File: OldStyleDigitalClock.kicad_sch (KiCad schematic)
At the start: 81 parts, among them SW1 Set minutes, SW2 Set hours, U1 D168K, U10 D168K, U11 CD4026BE, U12 D168K, U13 CD4026BE, U2 CD4026BE, U3 CD4060BE, U4 D168K, U5 CD4026BE, U6 CD4017BE, U7 CD4017BE, U8 CD4017BE, U9 4073, Y1 HC49 XTAL (32768 Hz)

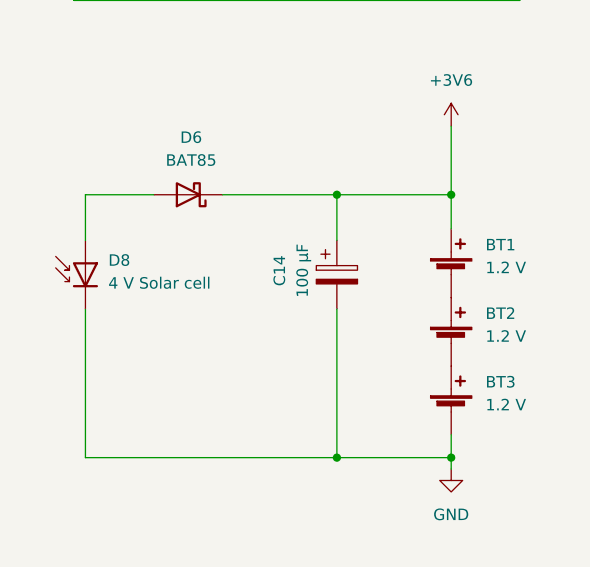
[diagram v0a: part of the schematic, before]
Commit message: Using 5 V solar cell instead of 4 V, as more appropriate for indoor situations
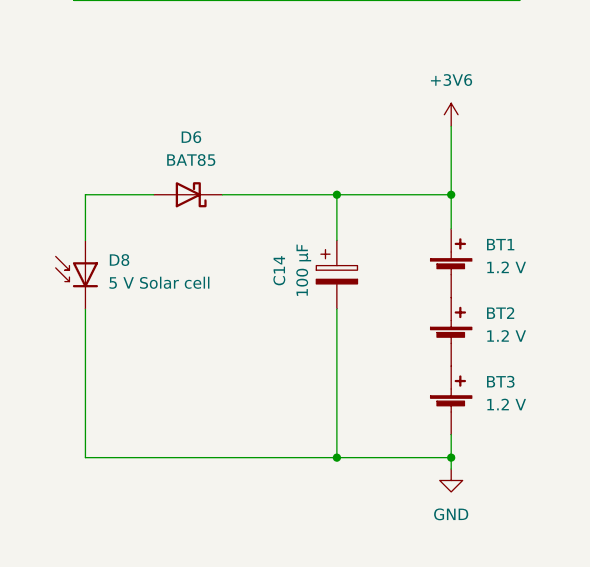
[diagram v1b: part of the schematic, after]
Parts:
- D8: value 4 V Solar cell -> 5 V Solar cell
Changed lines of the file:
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@@
       (effects (font (size 1.27 1.27)) (justify right))
     )
-    (property "Value" "4 V Solar cell" (id 1) (at 24.13 180.0224 90)
+    (property "Value" "5 V Solar cell" (id 1) (at 24.13 180.0224 90)
       (effects (font (size 1.27 1.27)) (justify right))
     )
@@
     )
     (path "/9a8343d9-4301-4fa0-a6a0-ed6d3137e10a"
-      (reference "D8") (unit 1) (value "4 V Solar cell") (footprint "TerminalBlock:TerminalBlock_bornier-2_P5.08mm")
+      (reference "D8") (unit 1) (value "5 V Solar cell") (footprint "TerminalBlock:TerminalBlock_bornier-2_P5.08mm")
     )
     (path "/0ff46600-2d15-4423-b669-8d7963d756aa"

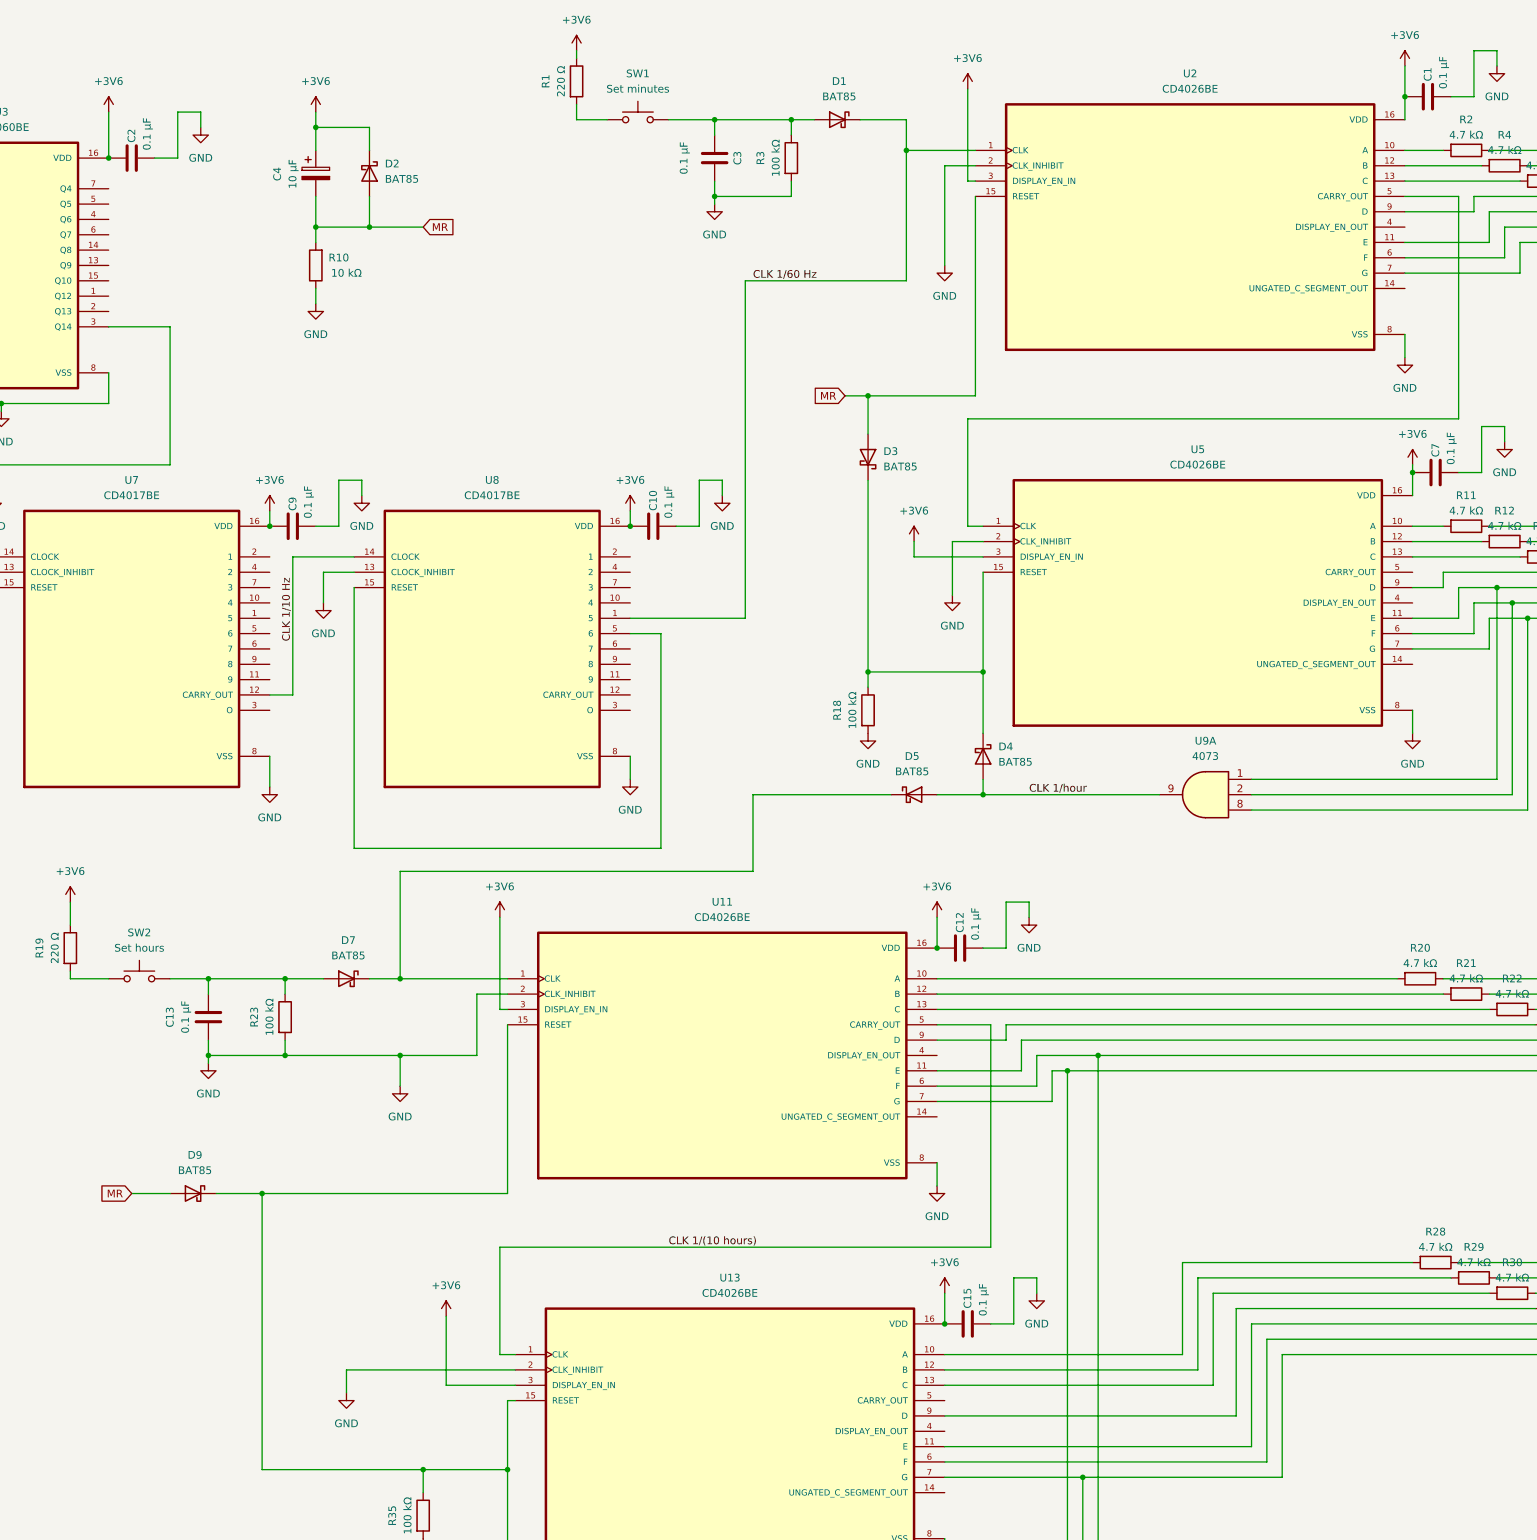
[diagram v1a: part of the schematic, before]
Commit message: Using 512 Hz clock signal to rapidly turn on and off the LEDs via the CD4026 display enable pin, both saving 50% power and hopefully improving the battery charging. The LED attenuation is negligible. This means than during the low state of the cycle, all the current from solar panels flows into the batteries, achieving a sort of trickle charging.
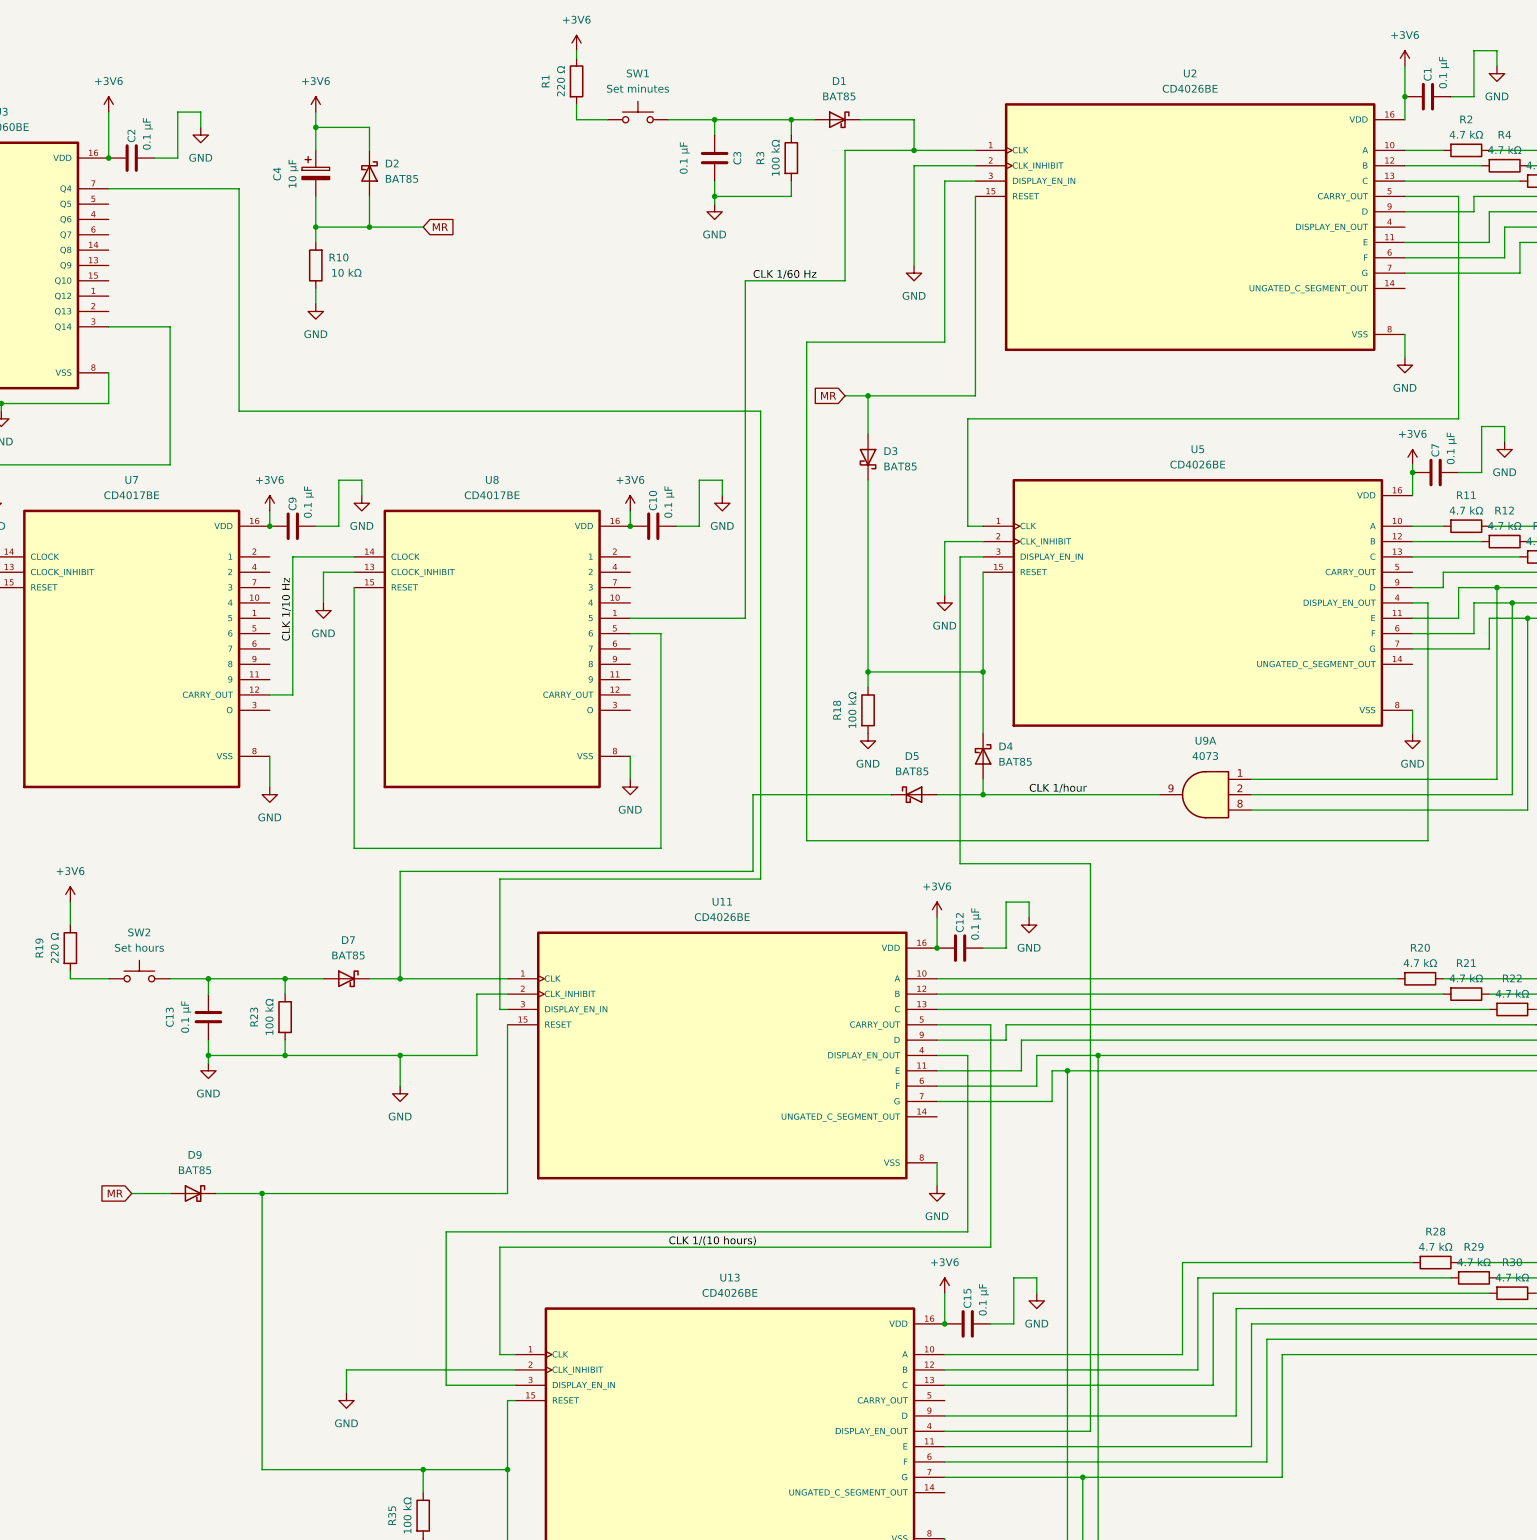
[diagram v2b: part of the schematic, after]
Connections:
- net VDD: no longer U11.3 (DISPLAY_EN_IN), U13.3 (DISPLAY_EN_IN), U2.3 (DISPLAY_EN_IN), U5.3 (DISPLAY_EN_IN)
- net at U11.4 (DISPLAY_EN_OUT): now also U13.3 (DISPLAY_EN_IN)
- net at U5.4 (DISPLAY_EN_OUT): now also U2.3 (DISPLAY_EN_IN)
- net at U13.4 (DISPLAY_EN_OUT): now also U5.3 (DISPLAY_EN_IN)
- net at U3.7 (Q4): now also U11.3 (DISPLAY_EN_IN)

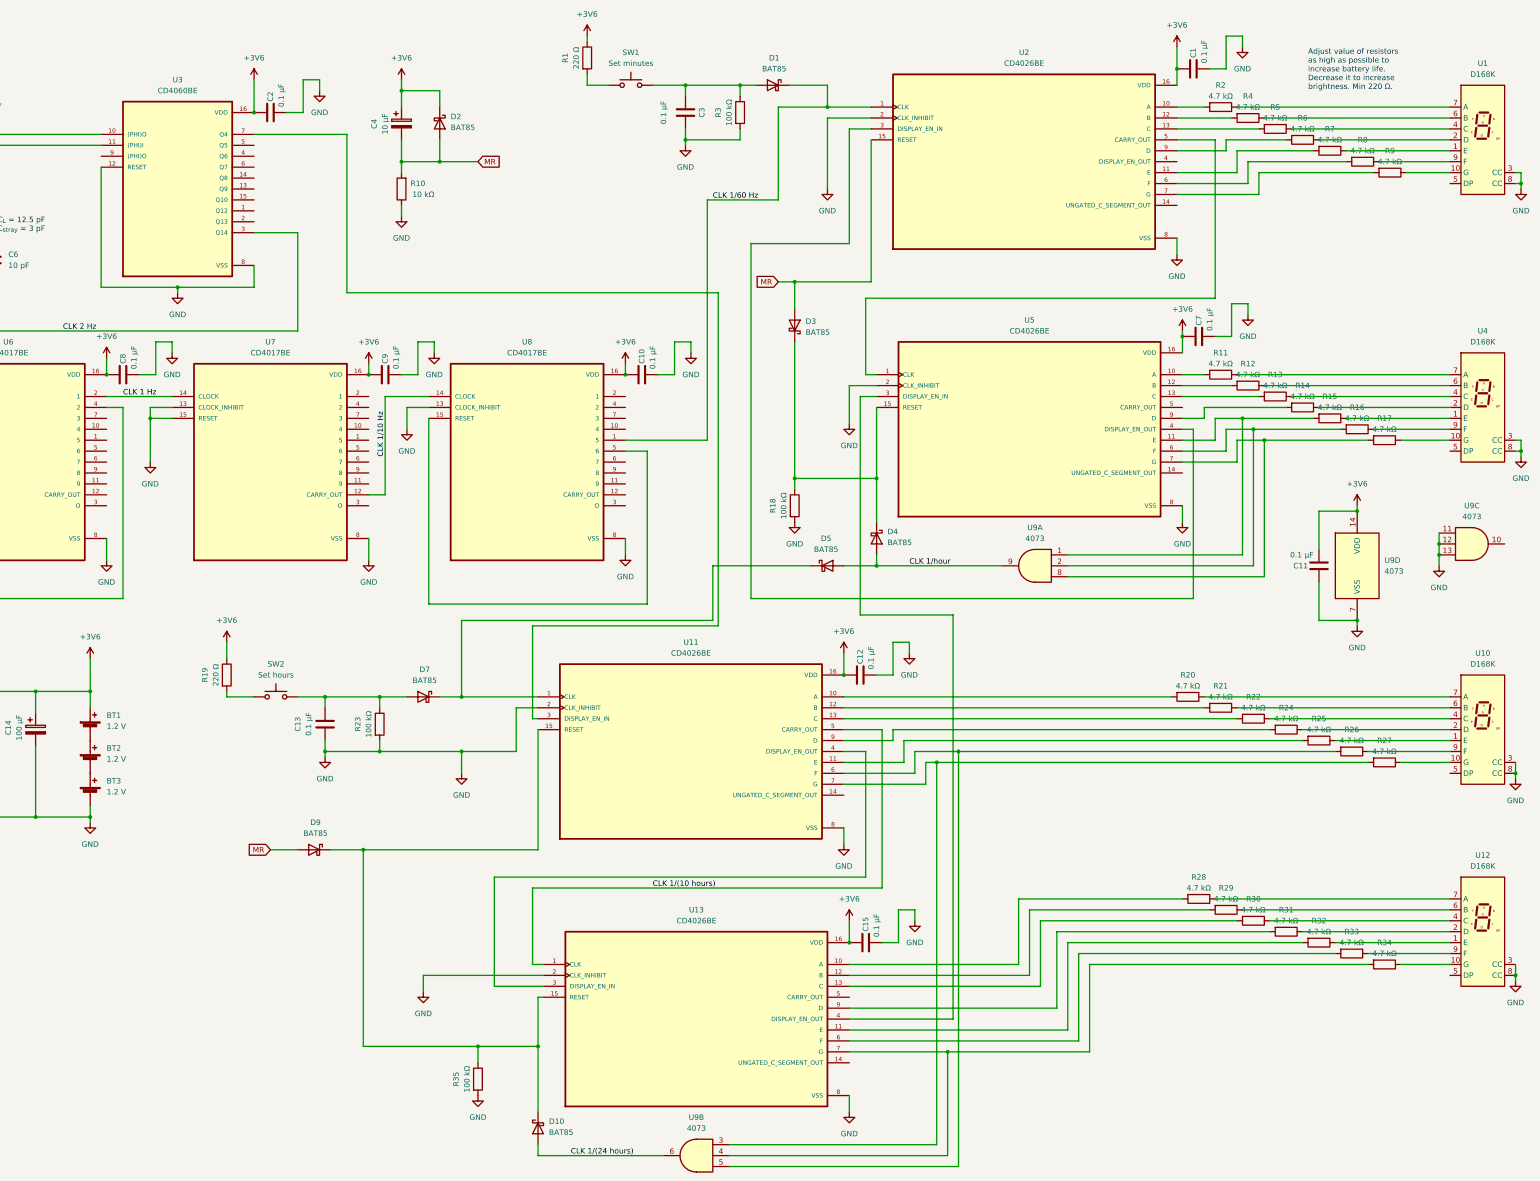
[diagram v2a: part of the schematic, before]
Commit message: Corrected LED display enable signal and decreased to 64 Hz to reduce capacitance and save power without any flickering visible
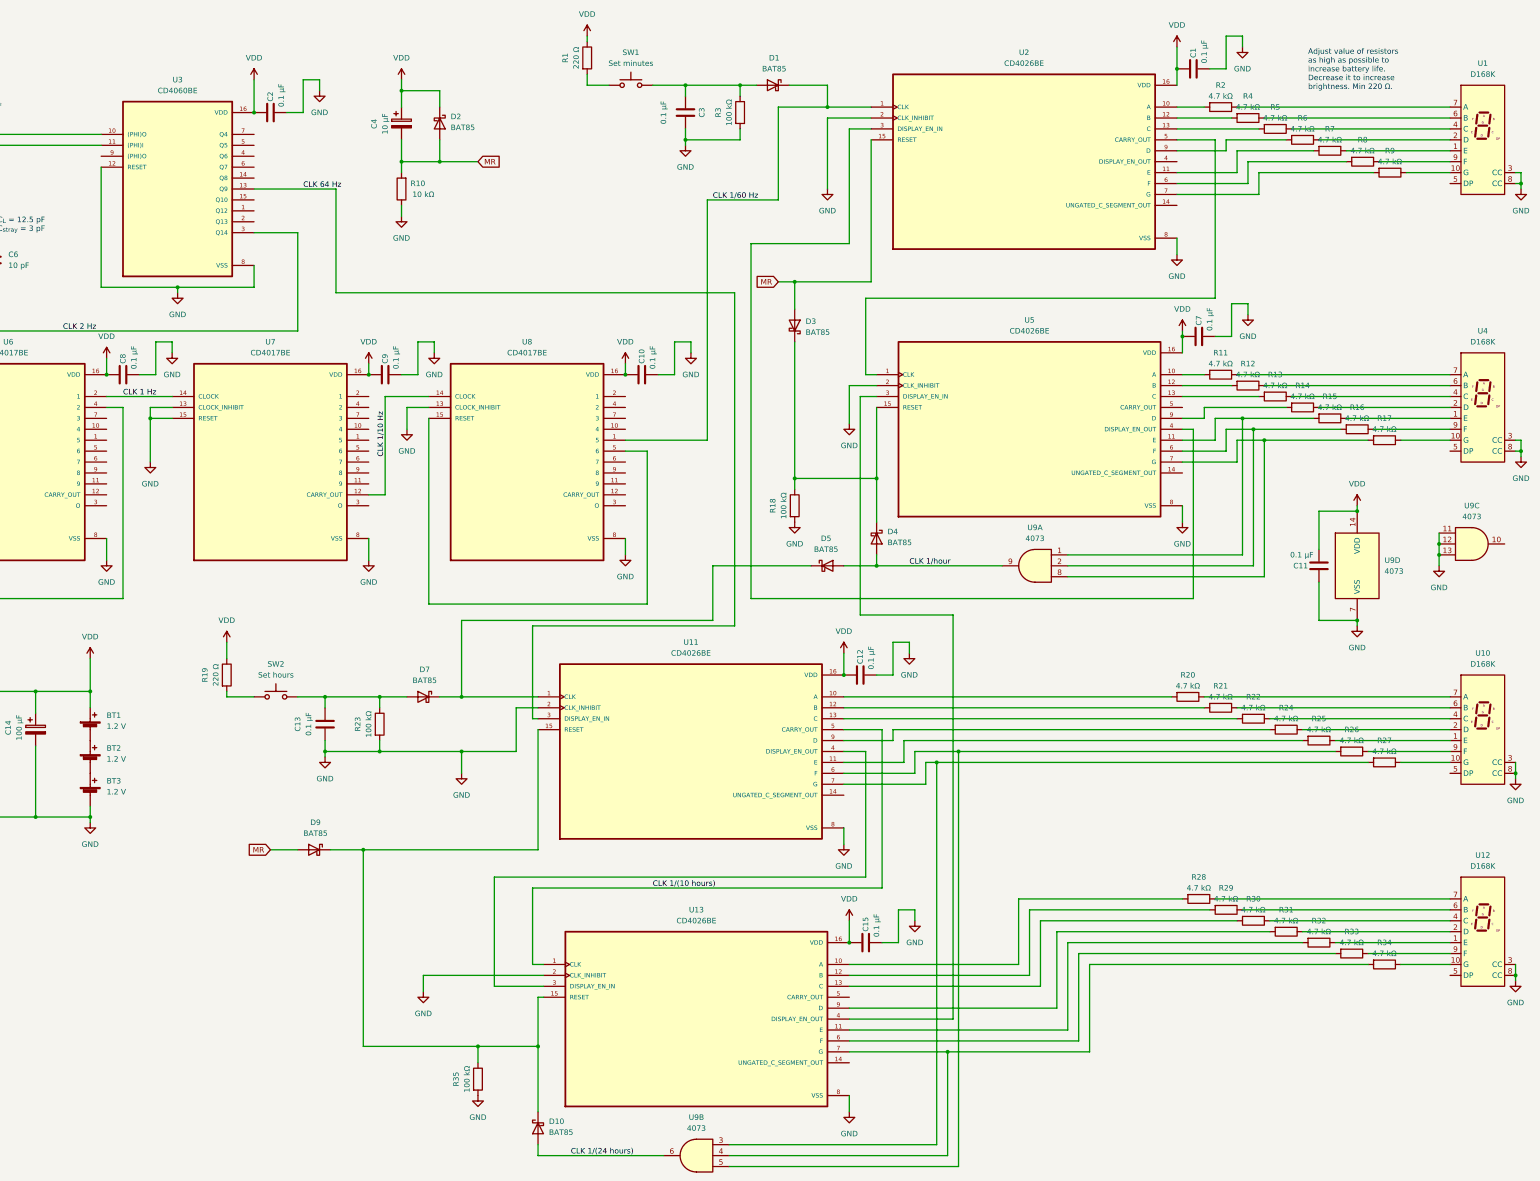
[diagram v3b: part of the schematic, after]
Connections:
- net at U3.7 (Q4): no longer U11.3 (DISPLAY_EN_IN)
- net CLK 64 Hz: now reaches U3.13 (Q9)
- net CLK 64 Hz: now also U11.3 (DISPLAY_EN_IN)
